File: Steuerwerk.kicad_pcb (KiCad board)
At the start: 2 copper layers, 100 x 160 mm, 225 parts, among them J1 Conn_01x04, J2 Conn_01x02, J3 Conn_01x03, J4 Conn_01x03, J5 Conn_01x02, J6 Conn_01x04, J7 Conn_01x02, J8 Conn_01x04, J9 Conn_01x02, Q1 Q_PNP_BCE, U1 74LS161, U2 74LS138, U3 74LS138, U4 74240, U5 74LS374, U6 74LS374, U7 74541, U8 74541

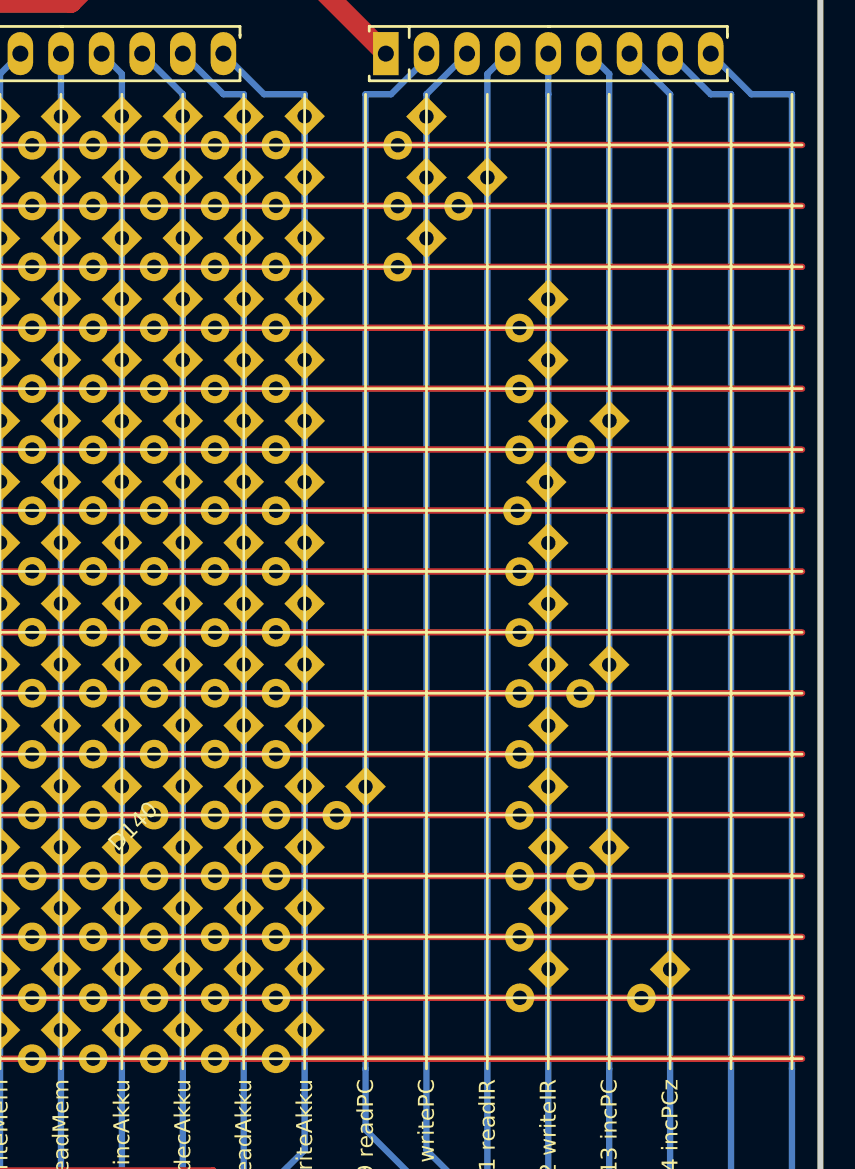
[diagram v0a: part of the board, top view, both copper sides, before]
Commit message: Steuerwerk: alle Diodenplatzhalter eingebaut
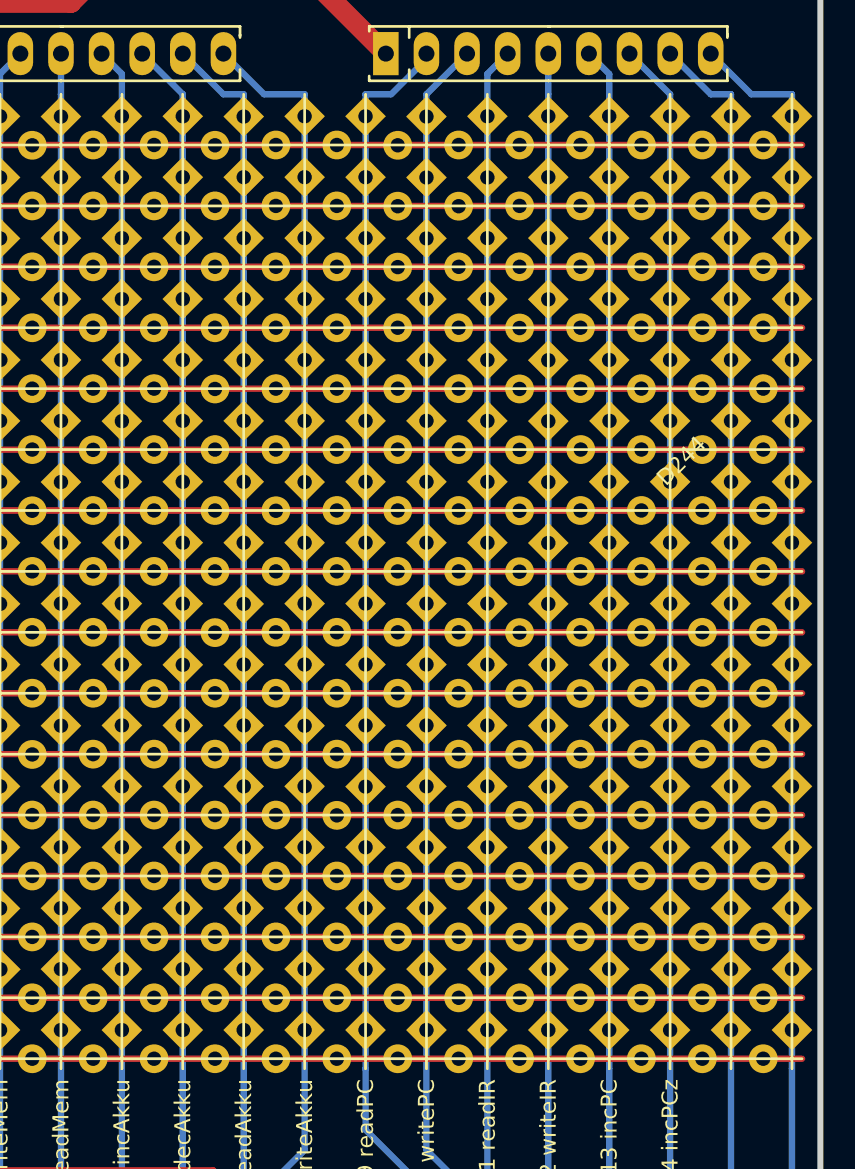
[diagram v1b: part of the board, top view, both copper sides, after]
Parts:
- added D173: bonsai_Led_Small_Platzhalter, bonsai:LED_Diodenmatrix_Platzhalter, F.Cu at (111.8, 56.6)
- added D174: bonsai_Led_Small_Platzhalter, bonsai:LED_Diodenmatrix_Platzhalter, F.Cu at (119.4, 56.6)
- added D175: bonsai_Led_Small_Platzhalter, bonsai:LED_Diodenmatrix_Platzhalter, F.Cu at (123.2, 56.6)
- added D176: bonsai_Led_Small_Platzhalter, bonsai:LED_Diodenmatrix_Platzhalter, F.Cu at (127.0, 56.6)
- added D177: bonsai_Led_Small_Platzhalter, bonsai:LED_Diodenmatrix_Platzhalter, F.Cu at (130.8, 56.6)
- added D178: bonsai_Led_Small_Platzhalter, bonsai:LED_Diodenmatrix_Platzhalter, F.Cu at (134.7, 56.6)
- added D179: bonsai_Led_Small_Platzhalter, bonsai:LED_Diodenmatrix_Platzhalter, F.Cu at (138.5, 56.6)
- added D180: bonsai_Led_Small_Platzhalter, bonsai:LED_Diodenmatrix_Platzhalter, F.Cu at (111.8, 60.4)
- added D181: bonsai_Led_Small_Platzhalter, bonsai:LED_Diodenmatrix_Platzhalter, F.Cu at (123.2, 60.4)
- added D182: bonsai_Led_Small_Platzhalter, bonsai:LED_Diodenmatrix_Platzhalter, F.Cu at (127.0, 60.4)
- added D183: bonsai_Led_Small_Platzhalter, bonsai:LED_Diodenmatrix_Platzhalter, F.Cu at (130.8, 60.4)
- added D184: bonsai_Led_Small_Platzhalter, bonsai:LED_Diodenmatrix_Platzhalter, F.Cu at (134.7, 60.4)
- added D185: bonsai_Led_Small_Platzhalter, bonsai:LED_Diodenmatrix_Platzhalter, F.Cu at (138.5, 60.4)
- added D186: bonsai_Led_Small_Platzhalter, bonsai:LED_Diodenmatrix_Platzhalter, F.Cu at (111.8, 64.2)
- added D187: bonsai_Led_Small_Platzhalter, bonsai:LED_Diodenmatrix_Platzhalter, F.Cu at (119.4, 64.2)
- added D188: bonsai_Led_Small_Platzhalter, bonsai:LED_Diodenmatrix_Platzhalter, F.Cu at (123.2, 64.2)
- added D189: bonsai_Led_Small_Platzhalter, bonsai:LED_Diodenmatrix_Platzhalter, F.Cu at (127.0, 64.2)
- added D190: bonsai_Led_Small_Platzhalter, bonsai:LED_Diodenmatrix_Platzhalter, F.Cu at (130.8, 64.2)
- added D191: bonsai_Led_Small_Platzhalter, bonsai:LED_Diodenmatrix_Platzhalter, F.Cu at (134.7, 64.2)
- added D192: bonsai_Led_Small_Platzhalter, bonsai:LED_Diodenmatrix_Platzhalter, F.Cu at (138.5, 64.2)
- added D193: bonsai_Led_Small_Platzhalter, bonsai:LED_Diodenmatrix_Platzhalter, F.Cu at (111.8, 68.0)
- added D194: bonsai_Led_Small_Platzhalter, bonsai:LED_Diodenmatrix_Platzhalter, F.Cu at (111.8, 71.8)
- added D195: bonsai_Led_Small_Platzhalter, bonsai:LED_Diodenmatrix_Platzhalter, F.Cu at (111.8, 75.6)
- added D196: bonsai_Led_Small_Platzhalter, bonsai:LED_Diodenmatrix_Platzhalter, F.Cu at (111.8, 79.4)
- added D197: bonsai_Led_Small_Platzhalter, bonsai:LED_Diodenmatrix_Platzhalter, F.Cu at (111.8, 83.3)
- added D198: bonsai_Led_Small_Platzhalter, bonsai:LED_Diodenmatrix_Platzhalter, F.Cu at (111.8, 87.1)
- added D199: bonsai_Led_Small_Platzhalter, bonsai:LED_Diodenmatrix_Platzhalter, F.Cu at (111.8, 90.9)
- added D200: bonsai_Led_Small_Platzhalter, bonsai:LED_Diodenmatrix_Platzhalter, F.Cu at (111.8, 94.7)
- added D201: bonsai_Led_Small_Platzhalter, bonsai:LED_Diodenmatrix_Platzhalter, F.Cu at (111.8, 102.3)
- added D202: bonsai_Led_Small_Platzhalter, bonsai:LED_Diodenmatrix_Platzhalter, F.Cu at (111.8, 106.1)
- added D203: bonsai_Led_Small_Platzhalter, bonsai:LED_Diodenmatrix_Platzhalter, F.Cu at (111.8, 109.9)
- added D204: bonsai_Led_Small_Platzhalter, bonsai:LED_Diodenmatrix_Platzhalter, F.Cu at (111.8, 113.7)
- added D205: bonsai_Led_Small_Platzhalter, bonsai:LED_Diodenmatrix_Platzhalter, F.Cu at (115.6, 68.0)
- added D206: bonsai_Led_Small_Platzhalter, bonsai:LED_Diodenmatrix_Platzhalter, F.Cu at (115.6, 71.8)
- added D207: bonsai_Led_Small_Platzhalter, bonsai:LED_Diodenmatrix_Platzhalter, F.Cu at (115.6, 75.6)
- added D208: bonsai_Led_Small_Platzhalter, bonsai:LED_Diodenmatrix_Platzhalter, F.Cu at (115.6, 79.4)
- added D209: bonsai_Led_Small_Platzhalter, bonsai:LED_Diodenmatrix_Platzhalter, F.Cu at (115.6, 83.3)
- added D210: bonsai_Led_Small_Platzhalter, bonsai:LED_Diodenmatrix_Platzhalter, F.Cu at (115.6, 87.1)
- added D211: bonsai_Led_Small_Platzhalter, bonsai:LED_Diodenmatrix_Platzhalter, F.Cu at (115.6, 90.9)
- added D212: bonsai_Led_Small_Platzhalter, bonsai:LED_Diodenmatrix_Platzhalter, F.Cu at (115.6, 94.7)
- added D213: bonsai_Led_Small_Platzhalter, bonsai:LED_Diodenmatrix_Platzhalter, F.Cu at (115.6, 98.5)
- added D214: bonsai_Led_Small_Platzhalter, bonsai:LED_Diodenmatrix_Platzhalter, F.Cu at (115.6, 102.3)
- added D215: bonsai_Led_Small_Platzhalter, bonsai:LED_Diodenmatrix_Platzhalter, F.Cu at (115.6, 106.1)
- added D216: bonsai_Led_Small_Platzhalter, bonsai:LED_Diodenmatrix_Platzhalter, F.Cu at (115.6, 109.9)
- added D217: bonsai_Led_Small_Platzhalter, bonsai:LED_Diodenmatrix_Platzhalter, F.Cu at (115.6, 113.7)
- added D218: bonsai_Led_Small_Platzhalter, bonsai:LED_Diodenmatrix_Platzhalter, F.Cu at (119.4, 68.0)
- added D219: bonsai_Led_Small_Platzhalter, bonsai:LED_Diodenmatrix_Platzhalter, F.Cu at (119.4, 71.8)
- added D220: bonsai_Led_Small_Platzhalter, bonsai:LED_Diodenmatrix_Platzhalter, F.Cu at (119.4, 75.6)
- added D221: bonsai_Led_Small_Platzhalter, bonsai:LED_Diodenmatrix_Platzhalter, F.Cu at (119.4, 79.4)
- added D222: bonsai_Led_Small_Platzhalter, bonsai:LED_Diodenmatrix_Platzhalter, F.Cu at (119.4, 83.3)
- added D223: bonsai_Led_Small_Platzhalter, bonsai:LED_Diodenmatrix_Platzhalter, F.Cu at (119.4, 87.1)
- added D224: bonsai_Led_Small_Platzhalter, bonsai:LED_Diodenmatrix_Platzhalter, F.Cu at (119.4, 90.9)
- added D225: bonsai_Led_Small_Platzhalter, bonsai:LED_Diodenmatrix_Platzhalter, F.Cu at (119.4, 94.7)
- added D226: bonsai_Led_Small_Platzhalter, bonsai:LED_Diodenmatrix_Platzhalter, F.Cu at (119.4, 98.5)
- added D227: bonsai_Led_Small_Platzhalter, bonsai:LED_Diodenmatrix_Platzhalter, F.Cu at (119.4, 102.3)
- added D228: bonsai_Led_Small_Platzhalter, bonsai:LED_Diodenmatrix_Platzhalter, F.Cu at (119.4, 106.1)
- added D229: bonsai_Led_Small_Platzhalter, bonsai:LED_Diodenmatrix_Platzhalter, F.Cu at (119.4, 109.9)
- added D230: bonsai_Led_Small_Platzhalter, bonsai:LED_Diodenmatrix_Platzhalter, F.Cu at (119.4, 113.7)
- added D231: bonsai_Led_Small_Platzhalter, bonsai:LED_Diodenmatrix_Platzhalter, F.Cu at (123.2, 113.7)
- added D232: bonsai_Led_Small_Platzhalter, bonsai:LED_Diodenmatrix_Platzhalter, F.Cu at (127.0, 68.0)
- added D233: bonsai_Led_Small_Platzhalter, bonsai:LED_Diodenmatrix_Platzhalter, F.Cu at (127.0, 71.8)
- added D234: bonsai_Led_Small_Platzhalter, bonsai:LED_Diodenmatrix_Platzhalter, F.Cu at (127.0, 79.4)
- added D235: bonsai_Led_Small_Platzhalter, bonsai:LED_Diodenmatrix_Platzhalter, F.Cu at (127.0, 83.3)
- added D236: bonsai_Led_Small_Platzhalter, bonsai:LED_Diodenmatrix_Platzhalter, F.Cu at (127.0, 87.1)
- added D237: bonsai_Led_Small_Platzhalter, bonsai:LED_Diodenmatrix_Platzhalter, F.Cu at (127.0, 94.7)
- added D238: bonsai_Led_Small_Platzhalter, bonsai:LED_Diodenmatrix_Platzhalter, F.Cu at (127.0, 98.5)
- added D239: bonsai_Led_Small_Platzhalter, bonsai:LED_Diodenmatrix_Platzhalter, F.Cu at (127.0, 106.1)
- added D240: bonsai_Led_Small_Platzhalter, bonsai:LED_Diodenmatrix_Platzhalter, F.Cu at (127.0, 109.9)
- added D241: bonsai_Led_Small_Platzhalter, bonsai:LED_Diodenmatrix_Platzhalter, F.Cu at (127.0, 113.7)
- added D242: bonsai_Led_Small_Platzhalter, bonsai:LED_Diodenmatrix_Platzhalter, F.Cu at (130.8, 68.0)
- added D243: bonsai_Led_Small_Platzhalter, bonsai:LED_Diodenmatrix_Platzhalter, F.Cu at (130.8, 71.8)
- added D244: bonsai_Led_Small_Platzhalter, bonsai:LED_Diodenmatrix_Platzhalter, F.Cu at (130.8, 75.6)
- added D245: bonsai_Led_Small_Platzhalter, bonsai:LED_Diodenmatrix_Platzhalter, F.Cu at (130.8, 79.4)
- added D246: bonsai_Led_Small_Platzhalter, bonsai:LED_Diodenmatrix_Platzhalter, F.Cu at (130.8, 83.3)
- added D247: bonsai_Led_Small_Platzhalter, bonsai:LED_Diodenmatrix_Platzhalter, F.Cu at (130.8, 87.1)
- added D248: bonsai_Led_Small_Platzhalter, bonsai:LED_Diodenmatrix_Platzhalter, F.Cu at (130.8, 90.9)
- added D249: bonsai_Led_Small_Platzhalter, bonsai:LED_Diodenmatrix_Platzhalter, F.Cu at (130.8, 94.7)
- added D250: bonsai_Led_Small_Platzhalter, bonsai:LED_Diodenmatrix_Platzhalter, F.Cu at (130.8, 98.5)
- added D251: bonsai_Led_Small_Platzhalter, bonsai:LED_Diodenmatrix_Platzhalter, F.Cu at (130.8, 102.3)
- added D252: bonsai_Led_Small_Platzhalter, bonsai:LED_Diodenmatrix_Platzhalter, F.Cu at (130.8, 106.1)
- added D253: bonsai_Led_Small_Platzhalter, bonsai:LED_Diodenmatrix_Platzhalter, F.Cu at (130.8, 113.7)
- added D254: bonsai_Led_Small_Platzhalter, bonsai:LED_Diodenmatrix_Platzhalter, F.Cu at (134.7, 68.0)
- added D255: bonsai_Led_Small_Platzhalter, bonsai:LED_Diodenmatrix_Platzhalter, F.Cu at (138.5, 68.0)
- added D256: bonsai_Led_Small_Platzhalter, bonsai:LED_Diodenmatrix_Platzhalter, F.Cu at (134.7, 71.8)
- added D257: bonsai_Led_Small_Platzhalter, bonsai:LED_Diodenmatrix_Platzhalter, F.Cu at (138.5, 71.8)
- added D258: bonsai_Led_Small_Platzhalter, bonsai:LED_Diodenmatrix_Platzhalter, F.Cu at (134.7, 75.6)
- added D259: bonsai_Led_Small_Platzhalter, bonsai:LED_Diodenmatrix_Platzhalter, F.Cu at (138.5, 75.6)
- added D260: bonsai_Led_Small_Platzhalter, bonsai:LED_Diodenmatrix_Platzhalter, F.Cu at (134.7, 79.4)
- added D261: bonsai_Led_Small_Platzhalter, bonsai:LED_Diodenmatrix_Platzhalter, F.Cu at (138.5, 79.4)
- added D262: bonsai_Led_Small_Platzhalter, bonsai:LED_Diodenmatrix_Platzhalter, F.Cu at (134.7, 83.3)
- added D263: bonsai_Led_Small_Platzhalter, bonsai:LED_Diodenmatrix_Platzhalter, F.Cu at (138.5, 83.3)
- added D264: bonsai_Led_Small_Platzhalter, bonsai:LED_Diodenmatrix_Platzhalter, F.Cu at (134.7, 87.1)
- added D265: bonsai_Led_Small_Platzhalter, bonsai:LED_Diodenmatrix_Platzhalter, F.Cu at (138.5, 87.1)
- added D266: bonsai_Led_Small_Platzhalter, bonsai:LED_Diodenmatrix_Platzhalter, F.Cu at (134.7, 90.9)
- added D267: bonsai_Led_Small_Platzhalter, bonsai:LED_Diodenmatrix_Platzhalter, F.Cu at (138.5, 90.9)
- added D268: bonsai_Led_Small_Platzhalter, bonsai:LED_Diodenmatrix_Platzhalter, F.Cu at (134.7, 94.7)
- added D269: bonsai_Led_Small_Platzhalter, bonsai:LED_Diodenmatrix_Platzhalter, F.Cu at (138.5, 94.7)
- added D270: bonsai_Led_Small_Platzhalter, bonsai:LED_Diodenmatrix_Platzhalter, F.Cu at (134.7, 98.5)
- added D271: bonsai_Led_Small_Platzhalter, bonsai:LED_Diodenmatrix_Platzhalter, F.Cu at (138.5, 98.5)
- added D272: bonsai_Led_Small_Platzhalter, bonsai:LED_Diodenmatrix_Platzhalter, F.Cu at (134.7, 102.3)
- added D273: bonsai_Led_Small_Platzhalter, bonsai:LED_Diodenmatrix_Platzhalter, F.Cu at (138.5, 102.3)
- added D274: bonsai_Led_Small_Platzhalter, bonsai:LED_Diodenmatrix_Platzhalter, F.Cu at (134.7, 106.1)
- added D275: bonsai_Led_Small_Platzhalter, bonsai:LED_Diodenmatrix_Platzhalter, F.Cu at (138.5, 106.1)
- added D276: bonsai_Led_Small_Platzhalter, bonsai:LED_Diodenmatrix_Platzhalter, F.Cu at (134.7, 109.9)
- added D277: bonsai_Led_Small_Platzhalter, bonsai:LED_Diodenmatrix_Platzhalter, F.Cu at (138.5, 109.9)
- added D278: bonsai_Led_Small_Platzhalter, bonsai:LED_Diodenmatrix_Platzhalter, F.Cu at (134.7, 113.7)
- added D279: bonsai_Led_Small_Platzhalter, bonsai:LED_Diodenmatrix_Platzhalter, F.Cu at (138.5, 113.7)
- moved D20 0.13 mm to (123.2, 79.5)
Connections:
- net /v0 renamed Net-(D10-Pad1)
- net /v1 renamed Net-(D100-Pad1)
- net /v10 renamed Net-(D174-Pad1)
- net /v11 renamed Net-(D11-Pad1)
- net /v12 renamed Net-(D17-Pad1)
- net /v13 renamed Net-(D177-Pad1)
- net /v14 renamed Net-(D178-Pad1)
- net /v15 renamed Net-(D179-Pad1)
- net /v2 renamed Net-(D101-Pad1)
- net /v3 renamed Net-(D102-Pad1)
- net /v4 renamed Net-(D108-Pad1)
- net /v5 renamed Net-(D103-Pad1)
- net /v6 renamed Net-(D104-Pad1)
- net /v7 renamed Net-(D105-Pad1)
- net /v8 renamed Net-(D173-Pad1)
- net /v9 renamed Net-(D205-Pad1)

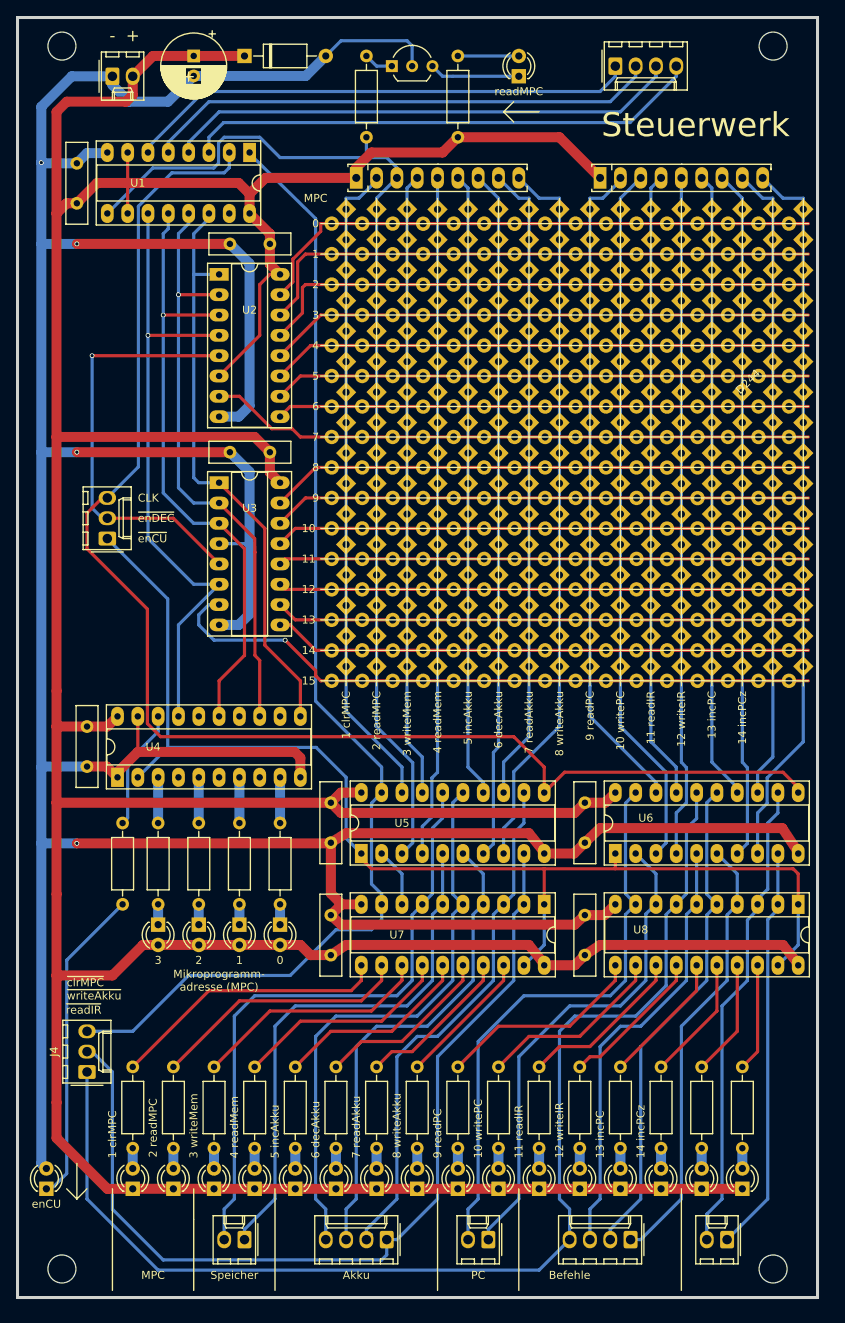
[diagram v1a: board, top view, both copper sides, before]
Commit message: Steuerwerk: EdgeCuts verschoben
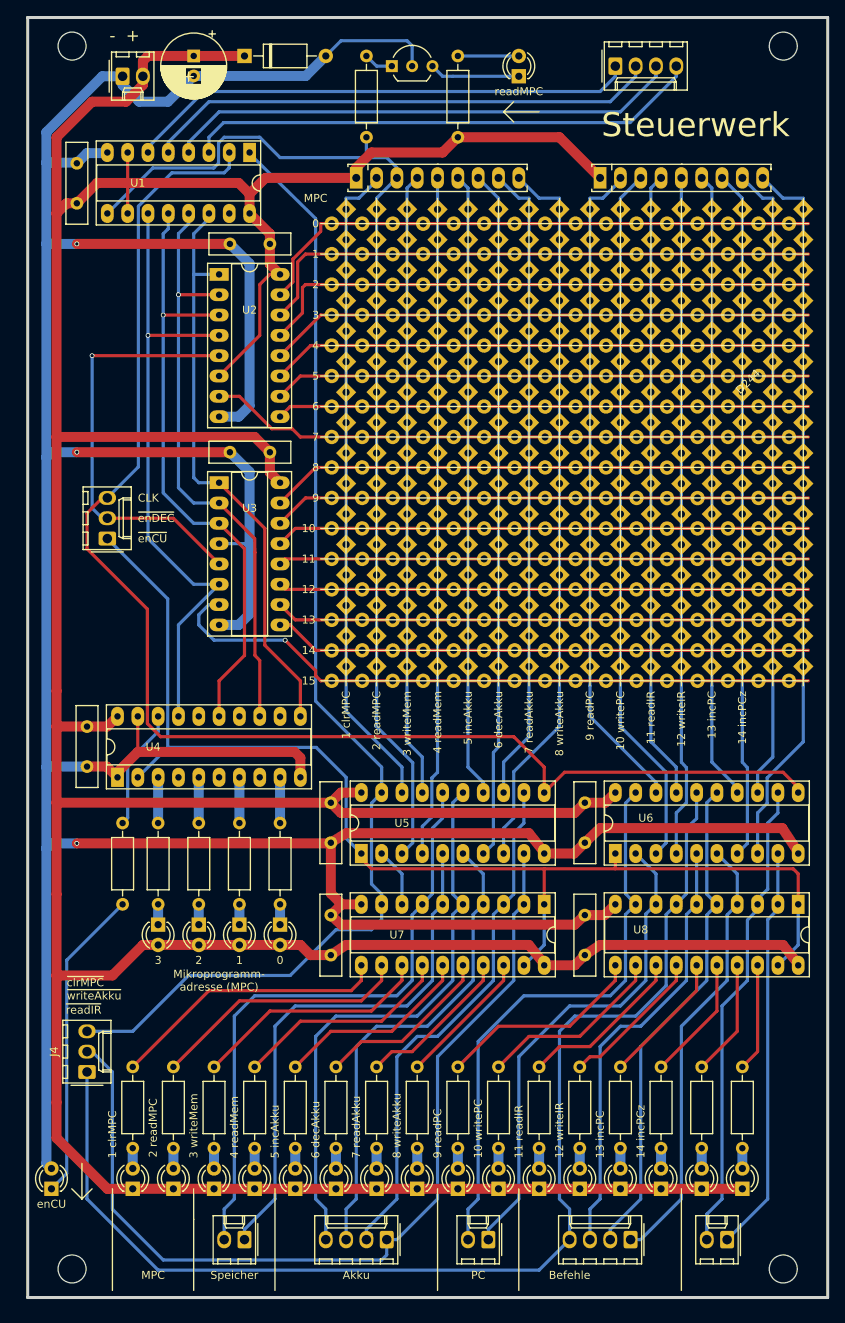
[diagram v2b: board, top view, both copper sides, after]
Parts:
- moved REF** 1.27 mm to (141.5, 192.6)
- moved J2 1.27 mm to (53.4, 40.0)
- moved D47 0.63 mm to (44.5, 179.0)
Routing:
- net GND: track 491.1 -> 486.0 mm, vias 4 -> 3
- net VCC: track 570.5 -> 569.1 mm
- net Net-(D47-Pad1): track 39.9 -> 39.2 mm

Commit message: Steuerwerk rev 2.0
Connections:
- net /Takt renamed /CLK
- net /clrMPC renamed /~clrMPC
- net /enAkku renamed /~writeAccu
- net /enDEC renamed /~enDEC
- net /enSTW renamed /~enCU
- net /loadIR renamed /~readR
- U4 pad 12: (no net) -> Net-(U4-Pad12)
- U4 pad 14: (no net) -> Net-(U4-Pad14)
- U4 pad 16: (no net) -> Net-(U4-Pad16)
- U4 pad 4: (no net) -> VCC
- U4 pad 6: (no net) -> VCC
- U4 pad 8: (no net) -> VCC
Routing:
- net VCC: track 569.1 -> 579.1 mm
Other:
- board text added: "5 incAccu"
- board text added: "6 decAccu"
- board text added: "7 readAccu"
- board text added: "8 writeAccu"
- board text added: "Accu"
- board text added: "rev 2.0"
- board text added: "~writeAccu"
- board text removed: "5 incAkku"
- board text removed: "6 decAkku"
- board text removed: "7 readAkku"
- board text removed: "8 writeAkku"
- board text removed: "Akku"
- board text removed: "~writeAkku"

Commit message: Steuerwerk und Befehle bearbeitet
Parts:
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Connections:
- D10 pad 1: Net-(D10-Pad1) -> /h6
- D10 pad 2: /h6 -> Net-(D10-Pad2)
- D100 pad 1: Net-(D100-Pad1) -> /h5
- D100 pad 2: /h5 -> Net-(D100-Pad2)
- D101 pad 1: Net-(D101-Pad1) -> /h5
- D101 pad 2: /h5 -> Net-(D101-Pad2)
- D102 pad 1: Net-(D102-Pad1) -> /h5
- D102 pad 2: /h5 -> Net-(D102-Pad2)
- D103 pad 1: Net-(D103-Pad1) -> /h5
- D103 pad 2: /h5 -> Net-(D103-Pad2)
- D104 pad 1: Net-(D104-Pad1) -> /h5
- D104 pad 2: /h5 -> Net-(D104-Pad2)
- D105 pad 1: Net-(D105-Pad1) -> /h5
- D105 pad 2: /h5 -> Net-(D105-Pad2)
- D106 pad 1: Net-(D100-Pad1) -> /h6
- D106 pad 2: /h6 -> Net-(D100-Pad2)
- D107 pad 1: Net-(D101-Pad1) -> /h6
- D107 pad 2: /h6 -> Net-(D101-Pad2)
- D108 pad 1: Net-(D108-Pad1) -> /h6
- D108 pad 2: /h6 -> Net-(D108-Pad2)
- D109 pad 1: Net-(D103-Pad1) -> /h6
- D109 pad 2: /h6 -> Net-(D103-Pad2)
- D11 pad 1: Net-(D11-Pad1) -> /h3
- D11 pad 2: /h3 -> Net-(D11-Pad2)
- D110 pad 1: Net-(D104-Pad1) -> /h6
- D110 pad 2: /h6 -> Net-(D104-Pad2)
- D111 pad 1: Net-(D10-Pad1) -> /h7
- D111 pad 2: /h7 -> Net-(D10-Pad2)
- D112 pad 1: Net-(D100-Pad1) -> /h7
- D112 pad 2: /h7 -> Net-(D100-Pad2)
- D113 pad 1: Net-(D101-Pad1) -> /h7
- D113 pad 2: /h7 -> Net-(D101-Pad2)
- D114 pad 1: Net-(D102-Pad1) -> /h7
- D114 pad 2: /h7 -> Net-(D102-Pad2)
- D115 pad 1: Net-(D108-Pad1) -> /h7
- D115 pad 2: /h7 -> Net-(D108-Pad2)
- D116 pad 1: Net-(D103-Pad1) -> /h7
- D116 pad 2: /h7 -> Net-(D103-Pad2)
- D117 pad 1: Net-(D104-Pad1) -> /h7
- D117 pad 2: /h7 -> Net-(D104-Pad2)
- D118 pad 1: Net-(D105-Pad1) -> /h7
- D118 pad 2: /h7 -> Net-(D105-Pad2)
- D119 pad 1: Net-(D10-Pad1) -> /h8
- D119 pad 2: /h8 -> Net-(D10-Pad2)
- D12 pad 1: Net-(D101-Pad1) -> /h4
- D12 pad 2: /h4 -> Net-(D101-Pad2)
- D120 pad 1: Net-(D100-Pad1) -> /h8
- D120 pad 2: /h8 -> Net-(D100-Pad2)
- D121 pad 1: Net-(D102-Pad1) -> /h8
- D121 pad 2: /h8 -> Net-(D102-Pad2)
- D122 pad 1: Net-(D108-Pad1) -> /h8
- D122 pad 2: /h8 -> Net-(D108-Pad2)
- D123 pad 1: Net-(D103-Pad1) -> /h8
- D123 pad 2: /h8 -> Net-(D103-Pad2)
- D124 pad 1: Net-(D105-Pad1) -> /h8
- D124 pad 2: /h8 -> Net-(D105-Pad2)
- D125 pad 1: Net-(D10-Pad1) -> /h9
- D125 pad 2: /h9 -> Net-(D10-Pad2)
- D126 pad 1: Net-(D100-Pad1) -> /h9
- D126 pad 2: /h9 -> Net-(D100-Pad2)
- D127 pad 1: Net-(D101-Pad1) -> /h9
- D127 pad 2: /h9 -> Net-(D101-Pad2)
- D128 pad 1: Net-(D102-Pad1) -> /h9
- D128 pad 2: /h9 -> Net-(D102-Pad2)
- D129 pad 1: Net-(D108-Pad1) -> /h9
- D129 pad 2: /h9 -> Net-(D108-Pad2)
- D13 pad 1: Net-(D104-Pad1) -> /h4
- D13 pad 2: /h4 -> Net-(D104-Pad2)
- D130 pad 1: Net-(D104-Pad1) -> /h9
- D130 pad 2: /h9 -> Net-(D104-Pad2)
- D131 pad 1: Net-(D105-Pad1) -> /h9
- D131 pad 2: /h9 -> Net-(D105-Pad2)
- D132 pad 1: Net-(D100-Pad1) -> /h10
- D132 pad 2: /h10 -> Net-(D100-Pad2)
- D133 pad 1: Net-(D101-Pad1) -> /h10
- D133 pad 2: /h10 -> Net-(D101-Pad2)
- D134 pad 1: Net-(D108-Pad1) -> /h10
- D134 pad 2: /h10 -> Net-(D108-Pad2)
- D135 pad 1: Net-(D103-Pad1) -> /h10
- D135 pad 2: /h10 -> Net-(D103-Pad2)
- D136 pad 1: Net-(D104-Pad1) -> /h10
- D136 pad 2: /h10 -> Net-(D104-Pad2)
- D137 pad 1: Net-(D100-Pad1) -> /h11
- D137 pad 2: /h11 -> Net-(D100-Pad2)
- D138 pad 1: Net-(D101-Pad1) -> /h11
- D138 pad 2: /h11 -> Net-(D101-Pad2)
- D139 pad 1: Net-(D102-Pad1) -> /h11
- D139 pad 2: /h11 -> Net-(D102-Pad2)
- D14 pad 1: Net-(D11-Pad1) -> /h4
- D14 pad 2: /h4 -> Net-(D11-Pad2)
- D140 pad 1: Net-(D108-Pad1) -> /h11
- D140 pad 2: /h11 -> Net-(D108-Pad2)
- D141 pad 1: Net-(D103-Pad1) -> /h11
- D141 pad 2: /h11 -> Net-(D103-Pad2)
- D142 pad 1: Net-(D104-Pad1) -> /h11
- D142 pad 2: /h11 -> Net-(D104-Pad2)
- D143 pad 1: Net-(D105-Pad1) -> /h11
- D143 pad 2: /h11 -> Net-(D105-Pad2)
- D144 pad 1: Net-(D10-Pad1) -> /h12
- D144 pad 2: /h12 -> Net-(D10-Pad2)
- D145 pad 1: Net-(D100-Pad1) -> /h12
- D145 pad 2: /h12 -> Net-(D100-Pad2)
- D146 pad 1: Net-(D101-Pad1) -> /h12
- D146 pad 2: /h12 -> Net-(D101-Pad2)
- D147 pad 1: Net-(D102-Pad1) -> /h12
- D147 pad 2: /h12 -> Net-(D102-Pad2)
- D148 pad 1: Net-(D108-Pad1) -> /h12
- D148 pad 2: /h12 -> Net-(D108-Pad2)
- D149 pad 1: Net-(D103-Pad1) -> /h12
- D149 pad 2: /h12 -> Net-(D103-Pad2)
- D15 pad 1: Net-(D108-Pad1) -> /h5
- D15 pad 2: /h5 -> Net-(D108-Pad2)
- D150 pad 1: Net-(D104-Pad1) -> /h12
- D150 pad 2: /h12 -> Net-(D104-Pad2)
- D151 pad 1: Net-(D105-Pad1) -> /h12
- D151 pad 2: /h12 -> Net-(D105-Pad2)
- D152 pad 1: Net-(D10-Pad1) -> /h13
- D152 pad 2: /h13 -> Net-(D10-Pad2)
- D153 pad 1: Net-(D100-Pad1) -> /h13
- D153 pad 2: /h13 -> Net-(D100-Pad2)
- D154 pad 1: Net-(D102-Pad1) -> /h13
- D154 pad 2: /h13 -> Net-(D102-Pad2)
- D155 pad 1: Net-(D108-Pad1) -> /h13
- D155 pad 2: /h13 -> Net-(D108-Pad2)
- D156 pad 1: Net-(D103-Pad1) -> /h13
- D156 pad 2: /h13 -> Net-(D103-Pad2)
- D157 pad 1: Net-(D104-Pad1) -> /h13
- D157 pad 2: /h13 -> Net-(D104-Pad2)
- D158 pad 1: Net-(D105-Pad1) -> /h13
- D158 pad 2: /h13 -> Net-(D105-Pad2)
- D159 pad 1: Net-(D100-Pad1) -> /h14
- D159 pad 2: /h14 -> Net-(D100-Pad2)
- D16 pad 1: Net-(D11-Pad1) -> /h5
- D16 pad 2: /h5 -> Net-(D11-Pad2)
- D160 pad 1: Net-(D102-Pad1) -> /h14
- D160 pad 2: /h14 -> Net-(D102-Pad2)
- D161 pad 1: Net-(D108-Pad1) -> /h14
- D161 pad 2: /h14 -> Net-(D108-Pad2)
- D162 pad 1: Net-(D103-Pad1) -> /h14
- D162 pad 2: /h14 -> Net-(D103-Pad2)
- D163 pad 1: Net-(D104-Pad1) -> /h14
- D163 pad 2: /h14 -> Net-(D104-Pad2)
- D164 pad 1: Net-(D105-Pad1) -> /h14
- D164 pad 2: /h14 -> Net-(D105-Pad2)
- D165 pad 1: Net-(D10-Pad1) -> /h15
- D165 pad 2: /h15 -> Net-(D10-Pad2)
- D166 pad 1: Net-(D100-Pad1) -> /h15
- D166 pad 2: /h15 -> Net-(D100-Pad2)
- D167 pad 1: Net-(D101-Pad1) -> /h15
- D167 pad 2: /h15 -> Net-(D101-Pad2)
- D168 pad 1: Net-(D102-Pad1) -> /h15
- D168 pad 2: /h15 -> Net-(D102-Pad2)
- D169 pad 1: Net-(D108-Pad1) -> /h15
- D169 pad 2: /h15 -> Net-(D108-Pad2)
- D17 pad 1: Net-(D17-Pad1) -> /h5
- D17 pad 2: /h5 -> Net-(D17-Pad2)
- D170 pad 1: Net-(D103-Pad1) -> /h15
- D170 pad 2: /h15 -> Net-(D103-Pad2)
- D171 pad 1: Net-(D104-Pad1) -> /h15
- D171 pad 2: /h15 -> Net-(D104-Pad2)
- D172 pad 1: Net-(D105-Pad1) -> /h15
- D172 pad 2: /h15 -> Net-(D105-Pad2)
- D173 pad 1: Net-(D173-Pad1) -> /h0
- D173 pad 2: /h0 -> Net-(D173-Pad2)
- D174 pad 1: Net-(D174-Pad1) -> /h0
- D174 pad 2: /h0 -> Net-(D174-Pad2)
- D175 pad 1: Net-(D11-Pad1) -> /h0
- D175 pad 2: /h0 -> Net-(D11-Pad2)
- D176 pad 1: Net-(D17-Pad1) -> /h0
- D176 pad 2: /h0 -> Net-(D17-Pad2)
- D177 pad 1: Net-(D177-Pad1) -> /h0
- D177 pad 2: /h0 -> Net-(D177-Pad2)
- D178 pad 1: Net-(D178-Pad1) -> /h0
- D178 pad 2: /h0 -> Net-(D178-Pad2)
- D179 pad 1: Net-(D179-Pad1) -> /h0
- D179 pad 2: /h0 -> Net-(D179-Pad2)
- D18 pad 1: Net-(D102-Pad1) -> /h6
- D18 pad 2: /h6 -> Net-(D102-Pad2)
- D180 pad 1: Net-(D173-Pad1) -> /h1
- D180 pad 2: /h1 -> Net-(D173-Pad2)
- D181 pad 1: Net-(D11-Pad1) -> /h1
- D181 pad 2: /h1 -> Net-(D11-Pad2)
- D182 pad 1: Net-(D17-Pad1) -> /h1
- D182 pad 2: /h1 -> Net-(D17-Pad2)
- D183 pad 1: Net-(D177-Pad1) -> /h1
- D183 pad 2: /h1 -> Net-(D177-Pad2)
- D184 pad 1: Net-(D178-Pad1) -> /h1
- D184 pad 2: /h1 -> Net-(D178-Pad2)
- D185 pad 1: Net-(D179-Pad1) -> /h1
- D185 pad 2: /h1 -> Net-(D179-Pad2)
- D186 pad 1: Net-(D173-Pad1) -> /h2
- D186 pad 2: /h2 -> Net-(D173-Pad2)
- D187 pad 1: Net-(D174-Pad1) -> /h2
- D187 pad 2: /h2 -> Net-(D174-Pad2)
- D188 pad 1: Net-(D11-Pad1) -> /h2
- D188 pad 2: /h2 -> Net-(D11-Pad2)
- D189 pad 1: Net-(D17-Pad1) -> /h2
- D189 pad 2: /h2 -> Net-(D17-Pad2)
- D19 pad 1: Net-(D105-Pad1) -> /h6
- D19 pad 2: /h6 -> Net-(D105-Pad2)
- D190 pad 1: Net-(D177-Pad1) -> /h2
- D190 pad 2: /h2 -> Net-(D177-Pad2)
- D191 pad 1: Net-(D178-Pad1) -> /h2
- D191 pad 2: /h2 -> Net-(D178-Pad2)
- D192 pad 1: Net-(D179-Pad1) -> /h2
- D192 pad 2: /h2 -> Net-(D179-Pad2)
- D193 pad 1: Net-(D173-Pad1) -> /h3
- D193 pad 2: /h3 -> Net-(D173-Pad2)
- D194 pad 1: Net-(D173-Pad1) -> /h4
- D194 pad 2: /h4 -> Net-(D173-Pad2)
- D195 pad 1: Net-(D173-Pad1) -> /h5
- D195 pad 2: /h5 -> Net-(D173-Pad2)
- D196 pad 1: Net-(D173-Pad1) -> /h6
- D196 pad 2: /h6 -> Net-(D173-Pad2)
- D197 pad 1: Net-(D173-Pad1) -> /h7
- D197 pad 2: /h7 -> Net-(D173-Pad2)
- D198 pad 1: Net-(D173-Pad1) -> /h8
- D198 pad 2: /h8 -> Net-(D173-Pad2)
- D199 pad 1: Net-(D173-Pad1) -> /h9
- D199 pad 2: /h9 -> Net-(D173-Pad2)
- D20 pad 1: Net-(D11-Pad1) -> /h6
- D20 pad 2: /h6 -> Net-(D11-Pad2)
- D200 pad 1: Net-(D173-Pad1) -> /h10
- D200 pad 2: /h10 -> Net-(D173-Pad2)
- D201 pad 1: Net-(D173-Pad1) -> /h12
- D201 pad 2: /h12 -> Net-(D173-Pad2)
- D202 pad 1: Net-(D173-Pad1) -> /h13
- D202 pad 2: /h13 -> Net-(D173-Pad2)
- D203 pad 1: Net-(D173-Pad1) -> /h14
- D203 pad 2: /h14 -> Net-(D173-Pad2)
- D204 pad 1: Net-(D173-Pad1) -> /h15
- D204 pad 2: /h15 -> Net-(D173-Pad2)
- D205 pad 1: Net-(D205-Pad1) -> /h3
- D205 pad 2: /h3 -> Net-(D205-Pad2)
- D206 pad 1: Net-(D205-Pad1) -> /h4
- D206 pad 2: /h4 -> Net-(D205-Pad2)
- D207 pad 1: Net-(D205-Pad1) -> /h5
- D207 pad 2: /h5 -> Net-(D205-Pad2)
- D208 pad 1: Net-(D205-Pad1) -> /h6
- D208 pad 2: /h6 -> Net-(D205-Pad2)
- D209 pad 1: Net-(D205-Pad1) -> /h7
- D209 pad 2: /h7 -> Net-(D205-Pad2)
- D21 pad 1: Net-(D11-Pad1) -> /h7
- D21 pad 2: /h7 -> Net-(D11-Pad2)
- D210 pad 1: Net-(D205-Pad1) -> /h8
- D210 pad 2: /h8 -> Net-(D205-Pad2)
- D211 pad 1: Net-(D205-Pad1) -> /h9
- D211 pad 2: /h9 -> Net-(D205-Pad2)
- D212 pad 1: Net-(D205-Pad1) -> /h10
- D212 pad 2: /h10 -> Net-(D205-Pad2)
- D213 pad 1: Net-(D205-Pad1) -> /h11
- D213 pad 2: /h11 -> Net-(D205-Pad2)
- D214 pad 1: Net-(D205-Pad1) -> /h12
- D214 pad 2: /h12 -> Net-(D205-Pad2)
- D215 pad 1: Net-(D205-Pad1) -> /h13
- D215 pad 2: /h13 -> Net-(D205-Pad2)
- D216 pad 1: Net-(D205-Pad1) -> /h14
- D216 pad 2: /h14 -> Net-(D205-Pad2)
- D217 pad 1: Net-(D205-Pad1) -> /h15
- D217 pad 2: /h15 -> Net-(D205-Pad2)
- D218 pad 1: Net-(D174-Pad1) -> /h3
- D218 pad 2: /h3 -> Net-(D174-Pad2)
- D219 pad 1: Net-(D174-Pad1) -> /h4
- D219 pad 2: /h4 -> Net-(D174-Pad2)
- D22 pad 1: Net-(D101-Pad1) -> /h8
- D22 pad 2: /h8 -> Net-(D101-Pad2)
- D220 pad 1: Net-(D174-Pad1) -> /h5
- D220 pad 2: /h5 -> Net-(D174-Pad2)
- D221 pad 1: Net-(D174-Pad1) -> /h6
- D221 pad 2: /h6 -> Net-(D174-Pad2)
- D222 pad 1: Net-(D174-Pad1) -> /h7
- D222 pad 2: /h7 -> Net-(D174-Pad2)
- D223 pad 1: Net-(D174-Pad1) -> /h8
- D223 pad 2: /h8 -> Net-(D174-Pad2)
- D224 pad 1: Net-(D174-Pad1) -> /h9
- D224 pad 2: /h9 -> Net-(D174-Pad2)
- D225 pad 1: Net-(D174-Pad1) -> /h10
- D225 pad 2: /h10 -> Net-(D174-Pad2)
- D226 pad 1: Net-(D174-Pad1) -> /h11
- D226 pad 2: /h11 -> Net-(D174-Pad2)
- D227 pad 1: Net-(D174-Pad1) -> /h12
- D227 pad 2: /h12 -> Net-(D174-Pad2)
- D228 pad 1: Net-(D174-Pad1) -> /h13
- D228 pad 2: /h13 -> Net-(D174-Pad2)
- D229 pad 1: Net-(D174-Pad1) -> /h14
- D229 pad 2: /h14 -> Net-(D174-Pad2)
- D23 pad 1: Net-(D104-Pad1) -> /h8
- D23 pad 2: /h8 -> Net-(D104-Pad2)
- D230 pad 1: Net-(D174-Pad1) -> /h15
- D230 pad 2: /h15 -> Net-(D174-Pad2)
- D231 pad 1: Net-(D11-Pad1) -> /h15
- D231 pad 2: /h15 -> Net-(D11-Pad2)
- D232 pad 1: Net-(D17-Pad1) -> /h3
- D232 pad 2: /h3 -> Net-(D17-Pad2)
- D233 pad 1: Net-(D17-Pad1) -> /h4
- D233 pad 2: /h4 -> Net-(D17-Pad2)
- D234 pad 1: Net-(D17-Pad1) -> /h6
- D234 pad 2: /h6 -> Net-(D17-Pad2)
- D235 pad 1: Net-(D17-Pad1) -> /h7
- D235 pad 2: /h7 -> Net-(D17-Pad2)
- D236 pad 1: Net-(D17-Pad1) -> /h8
- D236 pad 2: /h8 -> Net-(D17-Pad2)
- D237 pad 1: Net-(D17-Pad1) -> /h10
- D237 pad 2: /h10 -> Net-(D17-Pad2)
- D238 pad 1: Net-(D17-Pad1) -> /h11
- D238 pad 2: /h11 -> Net-(D17-Pad2)
- D239 pad 1: Net-(D17-Pad1) -> /h13
- D239 pad 2: /h13 -> Net-(D17-Pad2)
- D24 pad 1: Net-(D11-Pad1) -> /h8
- D24 pad 2: /h8 -> Net-(D11-Pad2)
- D240 pad 1: Net-(D17-Pad1) -> /h14
- D240 pad 2: /h14 -> Net-(D17-Pad2)
- D241 pad 1: Net-(D17-Pad1) -> /h15
- D241 pad 2: /h15 -> Net-(D17-Pad2)
- D242 pad 1: Net-(D177-Pad1) -> /h3
- D242 pad 2: /h3 -> Net-(D177-Pad2)
- D243 pad 1: Net-(D177-Pad1) -> /h4
- D243 pad 2: /h4 -> Net-(D177-Pad2)
- D244 pad 1: Net-(D177-Pad1) -> /h5
- D244 pad 2: /h5 -> Net-(D177-Pad2)
- D245 pad 1: Net-(D177-Pad1) -> /h6
- D245 pad 2: /h6 -> Net-(D177-Pad2)
- D246 pad 1: Net-(D177-Pad1) -> /h7
- D246 pad 2: /h7 -> Net-(D177-Pad2)
- D247 pad 1: Net-(D177-Pad1) -> /h8
- D247 pad 2: /h8 -> Net-(D177-Pad2)
- D248 pad 1: Net-(D177-Pad1) -> /h9
- D248 pad 2: /h9 -> Net-(D177-Pad2)
- D249 pad 1: Net-(D177-Pad1) -> /h10
- D249 pad 2: /h10 -> Net-(D177-Pad2)
- D25 pad 1: Net-(D103-Pad1) -> /h9
- D25 pad 2: /h9 -> Net-(D103-Pad2)
- D250 pad 1: Net-(D177-Pad1) -> /h11
- D250 pad 2: /h11 -> Net-(D177-Pad2)
- D251 pad 1: Net-(D177-Pad1) -> /h12
- D251 pad 2: /h12 -> Net-(D177-Pad2)
- D252 pad 1: Net-(D177-Pad1) -> /h13
- D252 pad 2: /h13 -> Net-(D177-Pad2)
- D253 pad 1: Net-(D177-Pad1) -> /h15
- D253 pad 2: /h15 -> Net-(D177-Pad2)
- D254 pad 1: Net-(D178-Pad1) -> /h3
- D254 pad 2: /h3 -> Net-(D178-Pad2)
- D255 pad 1: Net-(D179-Pad1) -> /h3
- D255 pad 2: /h3 -> Net-(D179-Pad2)
- D256 pad 1: Net-(D178-Pad1) -> /h4
- D256 pad 2: /h4 -> Net-(D178-Pad2)
- D257 pad 1: Net-(D179-Pad1) -> /h4
- D257 pad 2: /h4 -> Net-(D179-Pad2)
- D258 pad 1: Net-(D178-Pad1) -> /h5
- D258 pad 2: /h5 -> Net-(D178-Pad2)
- D259 pad 1: Net-(D179-Pad1) -> /h5
- D259 pad 2: /h5 -> Net-(D179-Pad2)
- D26 pad 1: Net-(D11-Pad1) -> /h9
- D26 pad 2: /h9 -> Net-(D11-Pad2)
- D260 pad 1: Net-(D178-Pad1) -> /h6
- D260 pad 2: /h6 -> Net-(D178-Pad2)
- D261 pad 1: Net-(D179-Pad1) -> /h6
- D261 pad 2: /h6 -> Net-(D179-Pad2)
- D262 pad 1: Net-(D178-Pad1) -> /h7
- D262 pad 2: /h7 -> Net-(D178-Pad2)
- D263 pad 1: Net-(D179-Pad1) -> /h7
- D263 pad 2: /h7 -> Net-(D179-Pad2)
- D264 pad 1: Net-(D178-Pad1) -> /h8
- D264 pad 2: /h8 -> Net-(D178-Pad2)
- D265 pad 1: Net-(D179-Pad1) -> /h8
- D265 pad 2: /h8 -> Net-(D179-Pad2)
- D266 pad 1: Net-(D178-Pad1) -> /h9
- D266 pad 2: /h9 -> Net-(D178-Pad2)
- D267 pad 1: Net-(D179-Pad1) -> /h9
- D267 pad 2: /h9 -> Net-(D179-Pad2)
- D268 pad 1: Net-(D178-Pad1) -> /h10
- D268 pad 2: /h10 -> Net-(D178-Pad2)
- D269 pad 1: Net-(D179-Pad1) -> /h10
- D269 pad 2: /h10 -> Net-(D179-Pad2)
- D27 pad 1: Net-(D17-Pad1) -> /h9
- D27 pad 2: /h9 -> Net-(D17-Pad2)
- D270 pad 1: Net-(D178-Pad1) -> /h11
- D270 pad 2: /h11 -> Net-(D178-Pad2)
- D271 pad 1: Net-(D179-Pad1) -> /h11
- D271 pad 2: /h11 -> Net-(D179-Pad2)
- D272 pad 1: Net-(D178-Pad1) -> /h12
- D272 pad 2: /h12 -> Net-(D178-Pad2)
- D273 pad 1: Net-(D179-Pad1) -> /h12
- D273 pad 2: /h12 -> Net-(D179-Pad2)
- D274 pad 1: Net-(D178-Pad1) -> /h13
- D274 pad 2: /h13 -> Net-(D178-Pad2)
- D275 pad 1: Net-(D179-Pad1) -> /h13
- D275 pad 2: /h13 -> Net-(D179-Pad2)
- D276 pad 1: Net-(D178-Pad1) -> /h14
- D276 pad 2: /h14 -> Net-(D178-Pad2)
- D277 pad 1: Net-(D179-Pad1) -> /h14
- D277 pad 2: /h14 -> Net-(D179-Pad2)
- D278 pad 1: Net-(D178-Pad1) -> /h15
- D278 pad 2: /h15 -> Net-(D178-Pad2)
- D279 pad 1: Net-(D179-Pad1) -> /h15
- D279 pad 2: /h15 -> Net-(D179-Pad2)
- D28 pad 1: Net-(D10-Pad1) -> /h10
- D28 pad 2: /h10 -> Net-(D10-Pad2)
- D29 pad 1: Net-(D102-Pad1) -> /h10
- D29 pad 2: /h10 -> Net-(D102-Pad2)
- D3 pad 1: Net-(D101-Pad1) -> /h1
- D3 pad 2: /h1 -> Net-(D101-Pad2)
- D30 pad 1: Net-(D105-Pad1) -> /h10
- D30 pad 2: /h10 -> Net-(D105-Pad2)
- D31 pad 1: Net-(D11-Pad1) -> /h10
- D31 pad 2: /h10 -> Net-(D11-Pad2)
- D32 pad 1: Net-(D10-Pad1) -> /h11
- D32 pad 2: /h11 -> Net-(D10-Pad2)
- D33 pad 1: Net-(D173-Pad1) -> /h11
- D33 pad 2: /h11 -> Net-(D173-Pad2)
- D34 pad 1: Net-(D11-Pad1) -> /h11
- D34 pad 2: /h11 -> Net-(D11-Pad2)
- D35 pad 1: Net-(D11-Pad1) -> /h12
- D35 pad 2: /h12 -> Net-(D11-Pad2)
- D36 pad 1: Net-(D17-Pad1) -> /h12
- D36 pad 2: /h12 -> Net-(D17-Pad2)
- D37 pad 1: Net-(D101-Pad1) -> /h13
- D37 pad 2: /h13 -> Net-(D101-Pad2)
- D38 pad 1: Net-(D11-Pad1) -> /h13
- D38 pad 2: /h13 -> Net-(D11-Pad2)
- D39 pad 1: Net-(D10-Pad1) -> /h14
- D39 pad 2: /h14 -> Net-(D10-Pad2)
- D4 pad 1: Net-(D205-Pad1) -> /h0
- D4 pad 2: /h0 -> Net-(D205-Pad2)
- D40 pad 1: Net-(D101-Pad1) -> /h14
- D40 pad 2: /h14 -> Net-(D101-Pad2)
- D41 pad 1: Net-(D11-Pad1) -> /h14
- D41 pad 2: /h14 -> Net-(D11-Pad2)
- D42 pad 1: Net-(D177-Pad1) -> /h14
- D42 pad 2: /h14 -> Net-(D177-Pad2)
- D47 pad 1: Net-(D47-Pad1) -> GND
- D47 pad 2: GND -> Net-(D47-Pad2)
- D48 pad 1: VCC -> Net-(D48-Pad1)
- D48 pad 2: Net-(D48-Pad2) -> VCC
- D49 pad 1: VCC -> Net-(D49-Pad1)
- D49 pad 2: Net-(D49-Pad2) -> VCC
- D5 pad 1: Net-(D205-Pad1) -> /h1
- D5 pad 2: /h1 -> Net-(D205-Pad2)
- D50 pad 1: VCC -> Net-(D50-Pad1)
- D50 pad 2: Net-(D50-Pad2) -> VCC
- D51 pad 1: VCC -> Net-(D51-Pad1)
- D51 pad 2: Net-(D51-Pad2) -> VCC
- D52 pad 1: VCC -> Net-(D52-Pad1)
- D52 pad 2: Net-(D52-Pad2) -> VCC
- D53 pad 1: VCC -> Net-(D53-Pad1)
- D53 pad 2: Net-(D53-Pad2) -> VCC
- D54 pad 1: VCC -> Net-(D54-Pad1)
- D54 pad 2: Net-(D54-Pad2) -> VCC
- D55 pad 1: VCC -> Net-(D55-Pad1)
- D55 pad 2: Net-(D55-Pad2) -> VCC
- D56 pad 1: VCC -> Net-(D56-Pad1)
- D56 pad 2: Net-(D56-Pad2) -> VCC
- D57 pad 1: VCC -> Net-(D57-Pad1)
- D57 pad 2: Net-(D57-Pad2) -> VCC
- D58 pad 1: VCC -> Net-(D58-Pad1)
- D58 pad 2: Net-(D58-Pad2) -> VCC
- D59 pad 1: VCC -> Net-(D59-Pad1)
- D59 pad 2: Net-(D59-Pad2) -> VCC
- D6 pad 1: Net-(D174-Pad1) -> /h1
- D6 pad 2: /h1 -> Net-(D174-Pad2)
- D60 pad 1: VCC -> Net-(D60-Pad1)
- D60 pad 2: Net-(D60-Pad2) -> VCC
- D61 pad 1: VCC -> Net-(D61-Pad1)
- D61 pad 2: Net-(D61-Pad2) -> VCC
- D62 pad 1: VCC -> Net-(D62-Pad1)
- D62 pad 2: Net-(D62-Pad2) -> VCC
- D63 pad 1: VCC -> Net-(D63-Pad1)
- D63 pad 2: Net-(D63-Pad2) -> VCC
- D64 pad 1: Net-(D10-Pad1) -> /h0
- D64 pad 2: /h0 -> Net-(D10-Pad2)
- D65 pad 1: Net-(D100-Pad1) -> /h0
- D65 pad 2: /h0 -> Net-(D100-Pad2)
- D66 pad 1: Net-(D101-Pad1) -> /h0
- D66 pad 2: /h0 -> Net-(D101-Pad2)
- D67 pad 1: Net-(D102-Pad1) -> /h0
- D67 pad 2: /h0 -> Net-(D102-Pad2)
- D68 pad 1: Net-(D108-Pad1) -> /h0
- D68 pad 2: /h0 -> Net-(D108-Pad2)
- D69 pad 1: Net-(D103-Pad1) -> /h0
- D69 pad 2: /h0 -> Net-(D103-Pad2)
- D7 pad 1: Net-(D100-Pad1) -> /h2
- D7 pad 2: /h2 -> Net-(D100-Pad2)
- D70 pad 1: Net-(D104-Pad1) -> /h0
- D70 pad 2: /h0 -> Net-(D104-Pad2)
- D71 pad 1: Net-(D105-Pad1) -> /h0
- D71 pad 2: /h0 -> Net-(D105-Pad2)
- D72 pad 1: Net-(D10-Pad1) -> /h1
- D72 pad 2: /h1 -> Net-(D10-Pad2)
- D73 pad 1: Net-(D100-Pad1) -> /h1
- D73 pad 2: /h1 -> Net-(D100-Pad2)
- D74 pad 1: Net-(D102-Pad1) -> /h1
- D74 pad 2: /h1 -> Net-(D102-Pad2)
- D75 pad 1: Net-(D108-Pad1) -> /h1
- D75 pad 2: /h1 -> Net-(D108-Pad2)
- D76 pad 1: Net-(D103-Pad1) -> /h1
- D76 pad 2: /h1 -> Net-(D103-Pad2)
- D77 pad 1: Net-(D104-Pad1) -> /h1
- D77 pad 2: /h1 -> Net-(D104-Pad2)
- D78 pad 1: Net-(D105-Pad1) -> /h1
- D78 pad 2: /h1 -> Net-(D105-Pad2)
- D79 pad 1: Net-(D10-Pad1) -> /h2
- D79 pad 2: /h2 -> Net-(D10-Pad2)
- D8 pad 1: Net-(D101-Pad1) -> /h2
- D8 pad 2: /h2 -> Net-(D101-Pad2)
- D80 pad 1: Net-(D102-Pad1) -> /h2
- D80 pad 2: /h2 -> Net-(D102-Pad2)
- D81 pad 1: Net-(D108-Pad1) -> /h2
- D81 pad 2: /h2 -> Net-(D108-Pad2)
- D82 pad 1: Net-(D103-Pad1) -> /h2
- D82 pad 2: /h2 -> Net-(D103-Pad2)
- D83 pad 1: Net-(D104-Pad1) -> /h2
- D83 pad 2: /h2 -> Net-(D104-Pad2)
- D84 pad 1: Net-(D105-Pad1) -> /h2
- D84 pad 2: /h2 -> Net-(D105-Pad2)
- D85 pad 1: Net-(D10-Pad1) -> /h3
- D85 pad 2: /h3 -> Net-(D10-Pad2)
- D86 pad 1: Net-(D100-Pad1) -> /h3
- D86 pad 2: /h3 -> Net-(D100-Pad2)
- D87 pad 1: Net-(D101-Pad1) -> /h3
- D87 pad 2: /h3 -> Net-(D101-Pad2)
- D88 pad 1: Net-(D102-Pad1) -> /h3
- D88 pad 2: /h3 -> Net-(D102-Pad2)
- D89 pad 1: Net-(D108-Pad1) -> /h3
- D89 pad 2: /h3 -> Net-(D108-Pad2)
- D9 pad 1: Net-(D205-Pad1) -> /h2
- D9 pad 2: /h2 -> Net-(D205-Pad2)
- D90 pad 1: Net-(D103-Pad1) -> /h3
- D90 pad 2: /h3 -> Net-(D103-Pad2)
- D91 pad 1: Net-(D104-Pad1) -> /h3
- D91 pad 2: /h3 -> Net-(D104-Pad2)
- D92 pad 1: Net-(D105-Pad1) -> /h3
- D92 pad 2: /h3 -> Net-(D105-Pad2)
- D93 pad 1: Net-(D10-Pad1) -> /h4
- D93 pad 2: /h4 -> Net-(D10-Pad2)
- D94 pad 1: Net-(D100-Pad1) -> /h4
- D94 pad 2: /h4 -> Net-(D100-Pad2)
- D95 pad 1: Net-(D102-Pad1) -> /h4
- D95 pad 2: /h4 -> Net-(D102-Pad2)
- D96 pad 1: Net-(D108-Pad1) -> /h4
- D96 pad 2: /h4 -> Net-(D108-Pad2)
- D97 pad 1: Net-(D103-Pad1) -> /h4
- D97 pad 2: /h4 -> Net-(D103-Pad2)
- D98 pad 1: Net-(D105-Pad1) -> /h4
- D98 pad 2: /h4 -> Net-(D105-Pad2)
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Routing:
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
